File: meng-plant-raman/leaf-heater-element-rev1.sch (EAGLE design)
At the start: 4 parts, among them IC1 MAX30205MTA+, X1 CON-JST2_SM05B-SRSS-TB

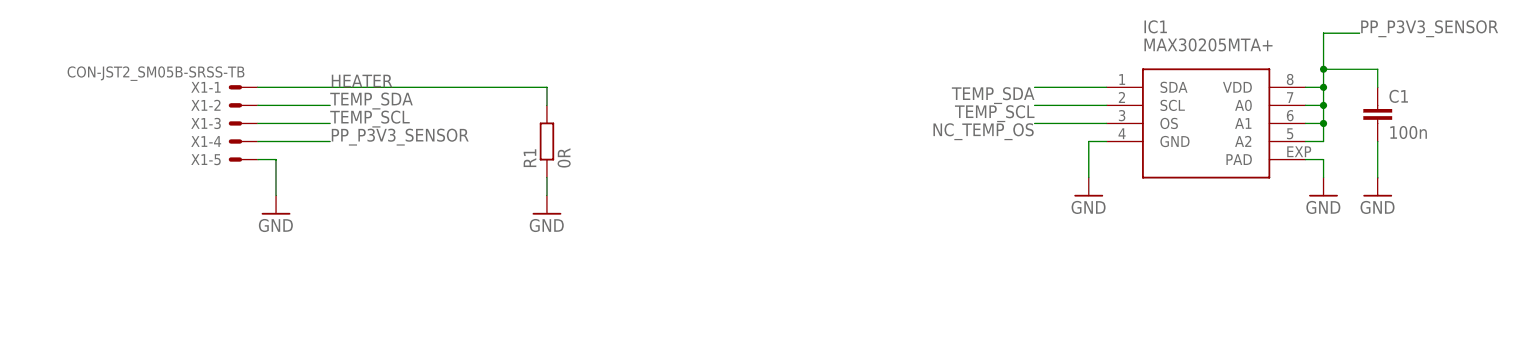
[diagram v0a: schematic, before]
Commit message: Updated leaf heaters with 6-pin JST SH
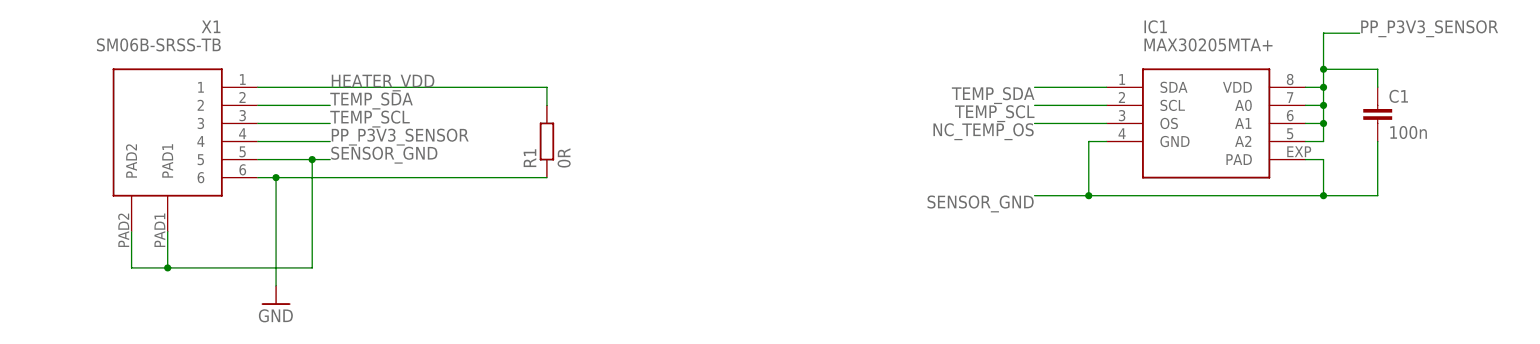
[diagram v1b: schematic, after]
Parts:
- X1: value CON-JST2_SM05B-SRSS-TB -> SM06B-SRSS-TB; device cheetah_driver_2:CON-JST2_SM05B-SRSS-TB -> meng-plant-raman:JST-SH-6PIN
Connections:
- removed net HEATER: R1.2, X1-1.S
- new net HEATER_VDD: R1.2, X1.1
- new net SENSOR_GND: C1.2, IC1.GND, IC1.PAD, X1.5, X1.PAD1, X1.PAD2
- net GND: now also X1.6; no longer C1.2, IC1.GND, IC1.PAD, X1-5.S
- net PP_P3V3_SENSOR: now also X1.4; no longer X1-4.S
- net TEMP_SCL: now also X1.3; no longer X1-3.S
- net TEMP_SDA: now also X1.2; no longer X1-2.S
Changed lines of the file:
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@@
 <?xml version="1.0" encoding="utf-8"?>
 <!DOCTYPE eagle SYSTEM "eagle.dtd">
-<eagle version="8.4.1">
+<eagle version="9.0.0">
 <drawing>
 <settings>
@@
 <part name="FRAME1" library="frames" library_urn="urn:adsk.eagle:library:229" deviceset="FRAME_A_L" device=""/>
 <part name="IC1" library="meng-plant-raman" deviceset="MAX30205" device="MTA+"/>
-<part name="GND1" library="supply1" library_urn="urn:adsk.eagle:library:371" deviceset="GND" device=""/>
 <part name="C1" library="rcl" library_urn="urn:adsk.eagle:library:334" deviceset="C-EU" device="C0402" package3d_urn="urn:adsk.eagle:package:23626/1" value="100n"/>
-<part name="GND3" library="supply1" library_urn="urn:adsk.eagle:library:371" deviceset="GND" device=""/>
-<part name="GND2" library="supply1" library_urn="urn:adsk.eagle:library:371" deviceset="GND" device=""/>
-<part name="X1" library="cheetah_driver_2" deviceset="CON-JST2_?M05B-SRSS-TB" device="S"/>
-<part name="GND4" library="supply1" library_urn="urn:adsk.eagle:library:371" deviceset="GND" device=""/>
 <part name="R1" library="rcl" library_urn="urn:adsk.eagle:library:334" deviceset="R-EU_" device="R0603" package3d_urn="urn:adsk.eagle:package:23555/2" value="0R"/>
+<part name="X1" library="meng-plant-raman" deviceset="JST-SH-6PIN" device="" value="SM06B-SRSS-TB"/>
 <part name="GND5" library="supply1" library_urn="urn:adsk.eagle:library:371" deviceset="GND" device=""/>
 </parts>
@@
 <instance part="FRAME1" gate="G$2" x="172.72" y="0"/>
 <instance part="IC1" gate="G$1" x="175.26" y="124.46"/>
-<instance part="GND1" gate="1" x="160.02" y="114.3"/>
 <instance part="C1" gate="G$1" x="200.66" y="127"/>
-<instance part="GND3" gate="1" x="200.66" y="114.3"/>
-<instance part="GND2" gate="1" x="193.04" y="114.3"/>
-<instance part="X1" gate="-1" x="40.64" y="129.54" rot="MR0"/>
-<instance part="X1" gate="-2" x="40.64" y="127" rot="MR0"/>
-<instance part="X1" gate="-3" x="40.64" y="124.46" rot="MR0"/>
-<instance part="X1" gate="-4" x="40.64" y="121.92" rot="MR0"/>
-<instance part="X1" gate="-5" x="40.64" y="119.38" rot="MR0"/>
-<instance part="GND4" gate="1" x="45.72" y="111.76"/>
 <instance part="R1" gate="G$1" x="83.82" y="121.92" rot="R90"/>
-<instance part="GND5" gate="1" x="83.82" y="111.76"/>
+<instance part="X1" gate="G$1" x="38.1" y="114.3" rot="MR0"/>
+<instance part="GND5" gate="1" x="45.72" y="99.06"/>
 </instances>
 <busses>
@@
 <net name="GND" class="0">
 <segment>
-<pinref part="GND1" gate="1" pin="GND"/>
-<wire x1="160.02" y1="116.84" x2="160.02" y2="121.92" width="0.1524" layer="91"/>
-<pinref part="IC1" gate="G$1" pin="GND"/>
-<wire x1="160.02" y1="121.92" x2="162.56" y2="121.92" width="0.1524" layer="91"/>
-</segment>
-<segment>
-<pinref part="GND3" gate="1" pin="GND"/>
-<wire x1="200.66" y1="116.84" x2="200.66" y2="121.92" width="0.1524" layer="91"/>
-<pinref part="C1" gate="G$1" pin="2"/>
-</segment>
-<segment>
-<pinref part="IC1" gate="G$1" pin="PAD"/>
-<wire x1="190.5" y1="119.38" x2="193.04" y2="119.38" width="0.1524" layer="91"/>
-<wire x1="193.04" y1="119.38" x2="193.04" y2="116.84" width="0.1524" layer="91"/>
-<pinref part="GND2" gate="1" pin="GND"/>
-</segment>
-<segment>
-<pinref part="X1" gate="-5" pin="S"/>
-<pinref part="GND4" gate="1" pin="GND"/>
-<wire x1="43.18" y1="119.38" x2="45.72" y2="119.38" width="0.1524" layer="91"/>
-<wire x1="45.72" y1="119.38" x2="45.72" y2="114.3" width="0.1524" layer="91"/>
-</segment>
-<segment>
 <pinref part="GND5" gate="1" pin="GND"/>
+<wire x1="45.72" y1="101.6" x2="45.72" y2="116.84" width="0.1524" layer="91"/>
+<pinref part="X1" gate="G$1" pin="6"/>
+<wire x1="45.72" y1="116.84" x2="43.18" y2="116.84" width="0.1524" layer="91"/>
 <pinref part="R1" gate="G$1" pin="1"/>
-<wire x1="83.82" y1="114.3" x2="83.82" y2="116.84" width="0.1524" layer="91"/>
+<wire x1="45.72" y1="116.84" x2="83.82" y2="116.84" width="0.1524" layer="91"/>
+<junction x="45.72" y="116.84"/>
 </segment>
 </net>
@@
 </segment>
 <segment>
-<pinref part="X1" gate="-4" pin="S"/>
 <wire x1="43.18" y1="121.92" x2="53.34" y2="121.92" width="0.1524" layer="91"/>
 <label x="53.34" y="121.92" size="1.778" layer="95"/>
+<pinref part="X1" gate="G$1" pin="4"/>
 </segment>
 </net>
@@
 </segment>
 <segment>
-<pinref part="X1" gate="-2" pin="S"/>
 <wire x1="43.18" y1="127" x2="53.34" y2="127" width="0.1524" layer="91"/>
 <label x="53.34" y="127" size="1.778" layer="95"/>
+<pinref part="X1" gate="G$1" pin="2"/>
 </segment>
 </net>
@@
 </segment>
 <segment>
-<pinref part="X1" gate="-3" pin="S"/>
 <wire x1="43.18" y1="124.46" x2="53.34" y2="124.46" width="0.1524" layer="91"/>
 <label x="53.34" y="124.46" size="1.778" layer="95"/>
+<pinref part="X1" gate="G$1" pin="3"/>
 </segment>
 </net>
@@
 </segment>
 </net>
-<net name="HEATER" class="0">
-<segment>
-<pinref part="X1" gate="-1" pin="S"/>
+<net name="HEATER_VDD" class="0">
+<segment>
 <label x="53.34" y="129.54" size="1.778" layer="95"/>
 <wire x1="43.18" y1="129.54" x2="83.82" y2="129.54" width="0.1524" layer="91"/>
 <wire x1="83.82" y1="129.54" x2="83.82" y2="127" width="0.1524" layer="91"/>
 <pinref part="R1" gate="G$1" pin="2"/>
-</segment>
-</net>
+<pinref part="X1" gate="G$1" pin="1"/>
+</segment>
+</net>
+<net name="SENSOR_GND" class="0">
+<segment>
+<pinref part="X1" gate="G$1" pin="5"/>
+<wire x1="43.18" y1="119.38" x2="50.8" y2="119.38" width="0.1524" layer="91"/>
+<label x="53.34" y="119.38" size="1.778" layer="95"/>
+<pinref part="X1" gate="G$1" pin="PAD2"/>
+<wire x1="50.8" y1="119.38" x2="53.34" y2="119.38" width="0.1524" layer="91"/>
+<wire x1="25.4" y1="109.22" x2="25.4" y2="104.14" width="0.1524" layer="91"/>
+<wire x1="25.4" y1="104.14" x2="30.48" y2="104.14" width="0.1524" layer="91"/>
+<pinref part="X1" gate="G$1" pin="PAD1"/>
+<wire x1="30.48" y1="104.14" x2="30.48" y2="109.22" width="0.1524" layer="91"/>
+<wire x1="30.48" y1="104.14" x2="50.8" y2="104.14" width="0.1524" layer="91"/>
+<wire x1="50.8" y1="104.14" x2="50.8" y2="119.38" width="0.1524" layer="91"/>
+<junction x="30.48" y="104.14"/>
+<junction x="50.8" y="119.38"/>
+</segment>
+<segment>
+<wire x1="160.02" y1="114.3" x2="160.02" y2="121.92" width="0.1524" layer="91"/>
+<pinref part="IC1" gate="G$1" pin="GND"/>
+<wire x1="160.02" y1="121.92" x2="162.56" y2="121.92" width="0.1524" layer="91"/>
+<wire x1="160.02" y1="114.3" x2="193.04" y2="114.3" width="0.1524" layer="91"/>
+<pinref part="IC1" gate="G$1" pin="PAD"/>
+<wire x1="190.5" y1="119.38" x2="193.04" y2="119.38" width="0.1524" layer="91"/>
+<wire x1="193.04" y1="114.3" x2="193.04" y2="119.38" width="0.1524" layer="91"/>
+<wire x1="193.04" y1="114.3" x2="200.66" y2="114.3" width="0.1524" layer="91"/>
+<wire x1="200.66" y1="114.3" x2="200.66" y2="121.92" width="0.1524" layer="91"/>
+<pinref part="C1" gate="G$1" pin="2"/>
+<wire x1="160.02" y1="114.3" x2="152.4" y2="114.3" width="0.1524" layer="91"/>
+<label x="152.4" y="114.3" size="1.778" layer="95" rot="R180"/>
+<junction x="160.02" y="114.3"/>
+<junction x="193.04" y="114.3"/>
+</segment>
+</net>
